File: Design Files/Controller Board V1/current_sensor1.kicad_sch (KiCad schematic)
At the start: 4 parts, among them U2 INA219BIDR

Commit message: resistor footprints
yuh
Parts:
- R1: footprint (none) -> Resistor_SMD:R_0805_2012Metric
- R2, R3: footprint (none) -> Resistor_SMD:R_0603_1608Metric
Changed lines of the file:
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@@
 			)
 		)
-		(property "Footprint" ""
+		(property "Footprint" "Resistor_SMD:R_0603_1608Metric"
 			(at 118.872 69.85 90)
 			(effects
@@
 			)
 		)
-		(property "Footprint" ""
+		(property "Footprint" "Resistor_SMD:R_0603_1608Metric"
 			(at 112.522 69.85 90)
 			(effects
@@
 			)
 		)
-		(property "Footprint" ""
+		(property "Footprint" "Resistor_SMD:R_0805_2012Metric"
 			(at 95.25 65.278 90)
 			(effects

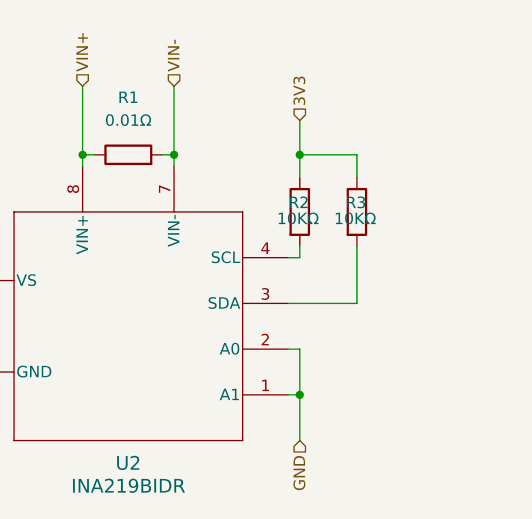
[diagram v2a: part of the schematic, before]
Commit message: I2C channels for pico and current sensors
gaming B)
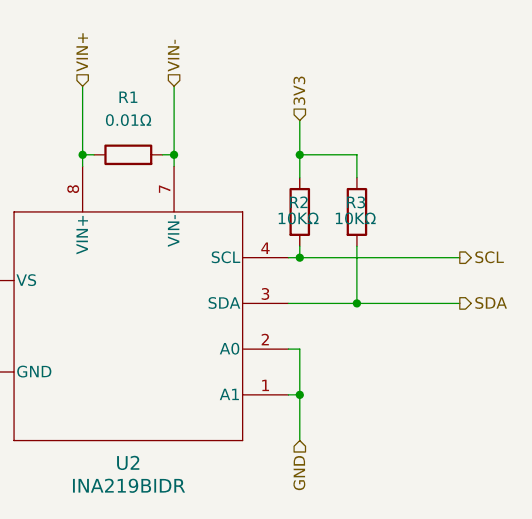
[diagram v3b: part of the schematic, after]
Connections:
- net SDA: now reaches R3.2, U2.3 (SDA)
- net SCL: now reaches R2.2, U2.4 (SCL)
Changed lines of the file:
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@@
+	)
+	(junction
+		(at 120.65 80.01)
+		(diameter 0)
+		(color 0 0 0 0)
 	)
 	(junction
@@
 		(color 0 0 0 0)
 	)
+	(junction
+		(at 114.3 74.93)
+		(diameter 0)
+		(color 0 0 0 0)
+	)
+	(wire
+		(pts
+			(xy 120.65 80.01) (xy 132.08 80.01)
+		)
+		(stroke
+			(width 0)
+			(type default)
+		)
+	)
 	(wire
 		(pts
@@
 	(wire
 		(pts
+			(xy 114.3 74.93) (xy 132.08 74.93)
+		)
+		(stroke
+			(width 0)
+			(type default)
+		)
+	)
+	(wire
+		(pts
 			(xy 113.03 80.01) (xy 120.65 80.01)
 		)
@@
 		(shape input)
 		(at 76.2 95.25 270)
+		(fields_autoplaced yes)
 		(effects
 			(font
@@
 		(shape input)
 		(at 90.17 55.88 90)
+		(fields_autoplaced yes)
 		(effects
 			(font
@@
 		(shape input)
 		(at 114.3 59.69 90)
+		(fields_autoplaced yes)
+		(effects
+			(font
+				(size 1.27 1.27)
+			)
+			(justify left)
+		)
+	)
+	(hierarchical_label "SCL"
+		(shape output)
+		(at 132.08 74.93 0)
+		(fields_autoplaced yes)
 		(effects
 			(font
@@
 		(shape input)
 		(at 76.2 69.85 90)
+		(fields_autoplaced yes)
 		(effects
 			(font
@@
 		(shape input)
 		(at 114.3 95.25 270)
+		(fields_autoplaced yes)
 		(effects
 			(font
@@
 		(shape input)
 		(at 100.33 55.88 90)
-		(effects
-			(font
+		(fields_autoplaced yes)
+		(effects
+			(font
+				(size 1.27 1.27)
+			)
+			(justify left)
+		)
+	)
+	(hierarchical_label "SDA"
+		(shape output)
+		(at 132.08 80.01 0)
+		(fields_autoplaced yes)
+		(effects
+			(font

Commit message: Assigning footprints and ading to schematic
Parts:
- renumbered R1 to R2, R2 to R3, R3 to R4
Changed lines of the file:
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@@
 		(shape input)
 		(at 76.2 95.25 270)
-		(fields_autoplaced yes)
 		(effects
 			(font
@@
 		(shape input)
 		(at 90.17 55.88 90)
-		(fields_autoplaced yes)
 		(effects
 			(font
@@
 		(shape input)
 		(at 114.3 59.69 90)
-		(fields_autoplaced yes)
 		(effects
 			(font
@@
 		(shape output)
 		(at 132.08 74.93 0)
-		(fields_autoplaced yes)
 		(effects
 			(font
@@
 		(shape input)
 		(at 76.2 69.85 90)
-		(fields_autoplaced yes)
 		(effects
 			(font
@@
 		(shape input)
 		(at 114.3 95.25 270)
-		(fields_autoplaced yes)
 		(effects
 			(font
@@
 		(shape input)
 		(at 100.33 55.88 90)
-		(fields_autoplaced yes)
 		(effects
 			(font
@@
 		(shape output)
 		(at 132.08 80.01 0)
-		(fields_autoplaced yes)
 		(effects
 			(font
@@
 		(on_board yes)
 		(dnp no)
-		(property "Reference" "R3"
+		(property "Reference" "R4"
 			(at 119.38 68.834 0)
 			(effects
@@
 			(project "Control Board V1"
 				(path "/e0c606b8-cbb9-4aff-b96c-73876da6ca74/39d380bc-529d-4f9d-86d0-4a47ae8ed980"
-					(reference "R3")
+					(reference "R4")
 					(unit 1)
 				)
@@
 		(on_board yes)
 		(dnp no)
-		(property "Reference" "R2"
+		(property "Reference" "R3"
 			(at 113.03 68.834 0)
 			(effects
@@
 			(project "Control Board V1"
 				(path "/e0c606b8-cbb9-4aff-b96c-73876da6ca74/39d380bc-529d-4f9d-86d0-4a47ae8ed980"
-					(reference "R2")
+					(reference "R3")
 					(unit 1)
 				)
@@
 		(dnp no)
 		(fields_autoplaced yes)
-		(property "Reference" "R1"
+		(property "Reference" "R2"
 			(at 95.25 57.15 90)
 			(effects
@@
 			(project "Control Board V1"
 				(path "/e0c606b8-cbb9-4aff-b96c-73876da6ca74/39d380bc-529d-4f9d-86d0-4a47ae8ed980"
-					(reference "R1")
+					(reference "R2")
 					(unit 1)
 				)

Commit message: Major Schematic Progress
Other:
- moved on the sheet: R2, R3, R4, U2

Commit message: here we go agane
Updating footprints and tackling general layout
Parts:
- added C4: 100 nF, Capacitor_SMD:C_0603_1608Metric, symbol Device:C
- U2: footprint D0008A_N -> Library:INA219
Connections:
- net 3V3: now also C4.1
- net GND: now also C4.2
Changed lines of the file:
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@@
 	(paper "A4")
 	(junction
+		(at 120.65 102.87)
+		(diameter 0)
+		(color 0 0 0 0)
+	)
+	(junction
 		(at 134.62 78.74)
 		(diameter 0)
@@
 	)
 	(junction
+		(at 120.65 92.71)
+		(diameter 0)
+		(color 0 0 0 0)
+	)
+	(junction
 		(at 158.75 78.74)
 		(diameter 0)
@@
 	(wire
 		(pts
+			(xy 120.65 101.6) (xy 120.65 102.87)
+		)
+		(stroke
+			(width 0)
+			(type default)
+		)
+	)
+	(wire
+		(pts
 			(xy 157.48 105.41) (xy 158.75 105.41)
 		)
@@
 		(pts
 			(xy 158.75 100.33) (xy 158.75 105.41)
+		)
+		(stroke
+			(width 0)
+			(type default)
+		)
+	)
+	(wire
+		(pts
+			(xy 120.65 92.71) (xy 120.65 93.98)
 		)
 		(stroke
@@
 			)
 			(justify left)
+		)
+	)
+	(symbol
+		(lib_id "Device:C")
+		(at 120.65 97.79 0)
+		(unit 1)
+		(exclude_from_sim no)
+		(in_bom yes)
+		(on_board yes)
+		(dnp no)
+		(fields_autoplaced yes)
+		(property "Reference" "C4"
+			(at 124.46 96.5199 0)
+			(effects
+				(font
+					(size 1.27 1.27)
+				)
+				(justify left)
+			)
+		)
+		(property "Value" "100 nF"
+			(at 124.46 99.0599 0)
+			(effects
+				(font
+					(size 1.27 1.27)
+				)
+				(justify left)
+			)
+		)
+		(property "Footprint" "Capacitor_SMD:C_0603_1608Metric"
+			(at 121.6152 101.6 0)
+			(effects
+				(font
+					(size 1.27 1.27)
+				)
+				(hide yes)
+			)
+		)
+		(property "Datasheet" "~"
+			(at 120.65 97.79 0)
+			(effects
+				(font
+					(size 1.27 1.27)
+				)
+				(hide yes)
+			)
+		)
+		(property "Description" "Unpolarized capacitor"
+			(at 120.65 97.79 0)
+			(effects
+				(font
+					(size 1.27 1.27)
+				)
+				(hide yes)
+			)
+		)
+		(property "MANUFACTURER" ""
+			(at 120.65 97.79 0)
+			(effects
+				(font
+					(size 1.27 1.27)
+				)
+				(hide yes)
+			)
+		)
+		(property "MAXIMUM_PACKAGE_HEIGHT" ""
+			(at 120.65 97.79 0)
+			(effects
+				(font
+					(size 1.27 1.27)
+				)
+				(hide yes)
+			)
+		)
+		(property "PARTREV" ""
+			(at 120.65 97.79 0)
+			(effects
+				(font
+					(size 1.27 1.27)
+				)
+				(hide yes)
+			)
+		)
+		(property "SNAPEDA_PN" ""
+			(at 120.65 97.79 0)
+			(effects
+				(font
+					(size 1.27 1.27)
+				)
+				(hide yes)
+			)
+		)
+		(property "STANDARD" ""
+			(at 120.65 97.79 0)
+			(effects
+				(font
+					(size 1.27 1.27)
+				)
+				(hide yes)
+			)
+		)
+		(pin "1"
+		)
+		(pin "2"
+		)
+		(instances
+			(project "Control Board V1"
+				(path "/e0c606b8-cbb9-4aff-b96c-73876da6ca74/39d380bc-529d-4f9d-86d0-4a47ae8ed980"
+					(reference "C4")
+					(unit 1)
+				)
+			)
 		)
 	)
@@
 			)
 		)
-		(property "Footprint" "D0008A_N"
+		(property "Footprint" "Library:INA219"
 			(at 139.7 97.79 0)
 			(effects
